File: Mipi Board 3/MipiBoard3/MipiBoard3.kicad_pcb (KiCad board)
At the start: 4 copper layers, 55 x 45 mm, 51 parts, among them J1 Power/Control Top, J2 Bank A Top, J3 Bank B Top, J4 MIPI1, J5 MIPI2, J6 Bank A Bottom, J7 Bank B Bottom, J8 Power/Control Bottom, U1 LM339, U2 LM339, U3 LM339

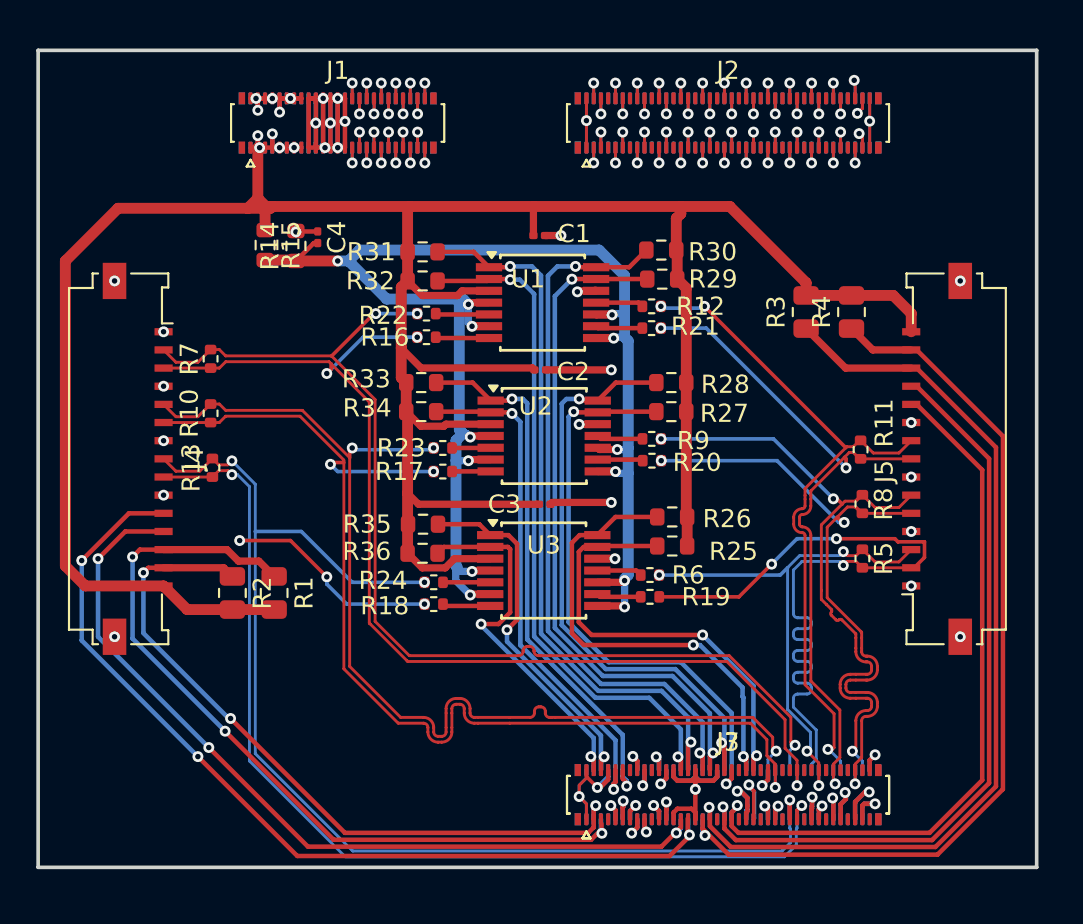
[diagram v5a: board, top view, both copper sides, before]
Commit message: Finished wiring and board adjustment
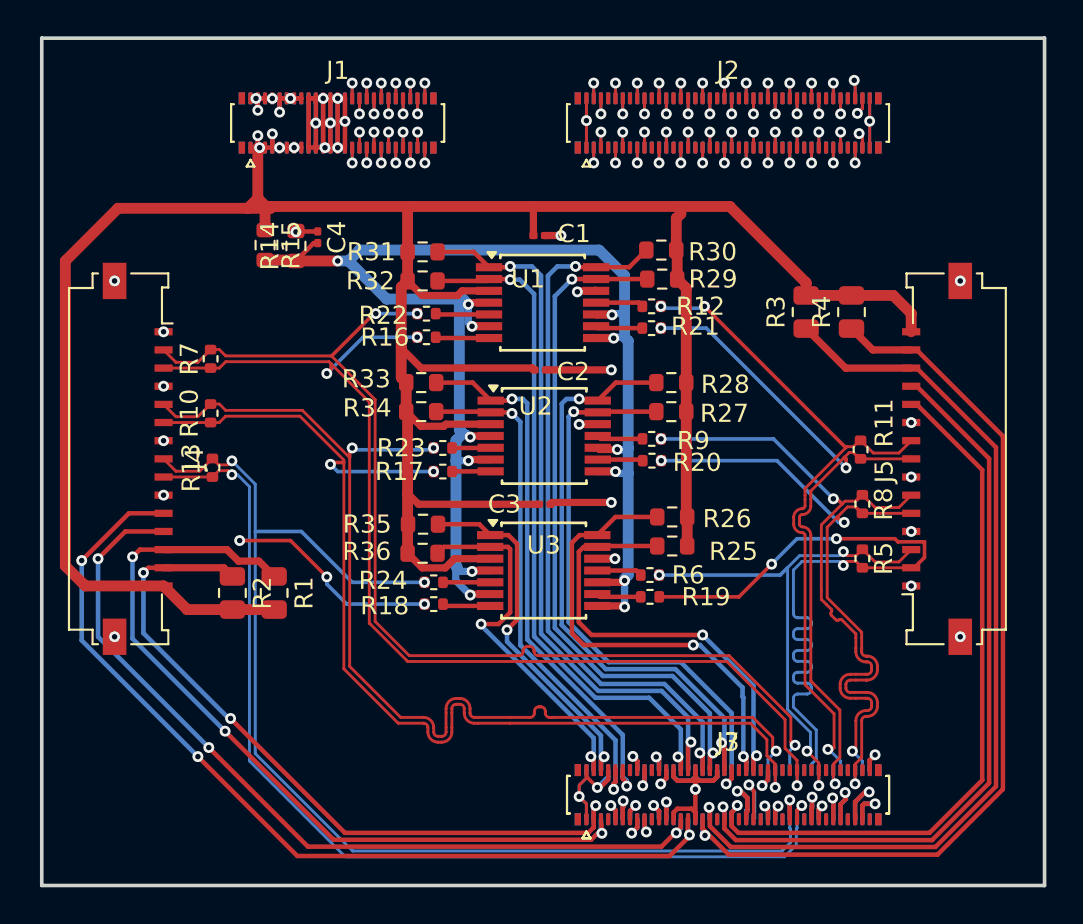
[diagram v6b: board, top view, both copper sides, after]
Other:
- board size 55 x 45 mm -> 55.2 x 46.7 mm
